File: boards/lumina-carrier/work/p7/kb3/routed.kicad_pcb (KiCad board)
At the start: 4 copper layers, 100 x 80 mm, 116 parts, among them J1 LPJG0926HENL PoE+ RJ45 magjack, J2 1x6 2.54mm header (recovery), J3 DS1021-2x7SF11-B 2x7 male hea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, J4 DS1021-2x12SF11-B 2x12 male h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, SW1 SMD tactile switch, U1 TPS2378DDAR, U10 W5500, U20 SCT2A25STER, U21 TPS563201DDCR, U22 TPS16630PWPR, U30 ESP32-S3-WROOM-1-N8, Y10 25MHz 18pF CL crystal

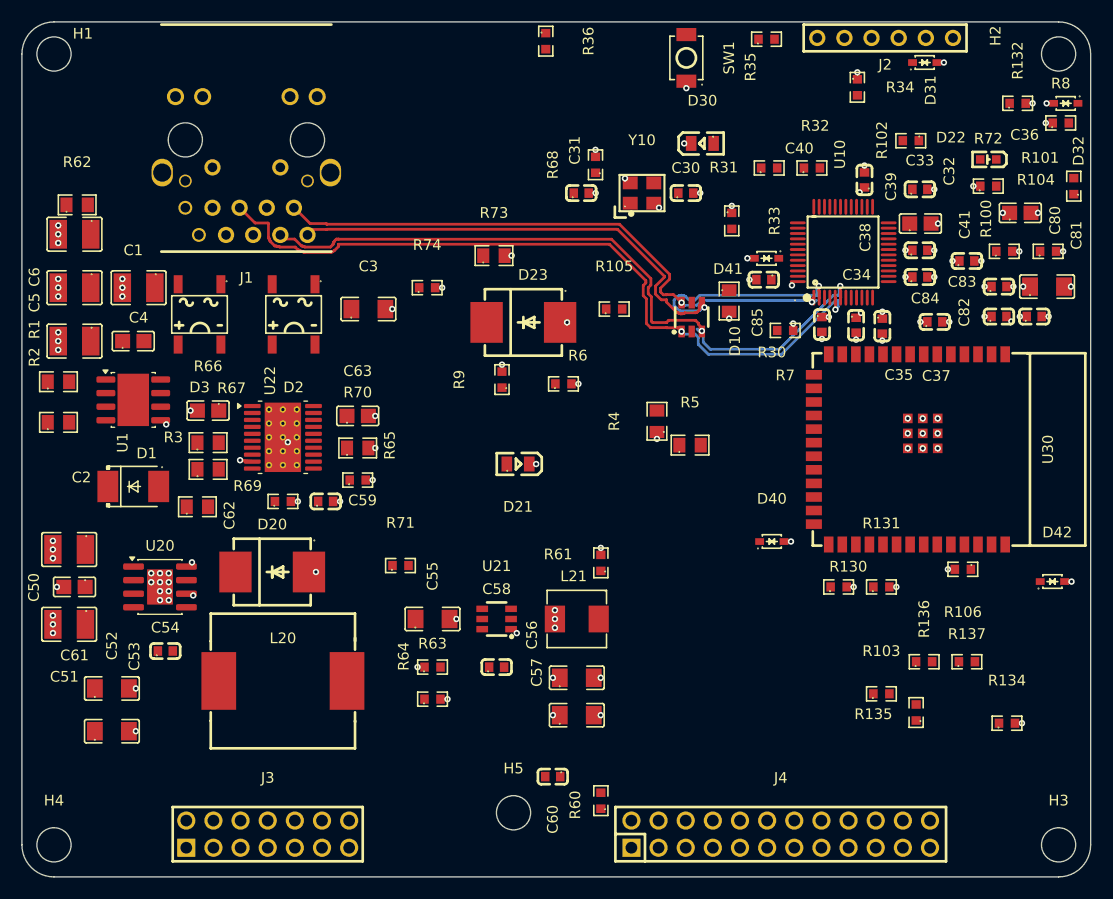
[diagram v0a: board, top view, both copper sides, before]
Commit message: ai-ee lumina-carrier: P7 partial - planes, rule areas, MDI pairs, thermal stitching (177 unrouted)
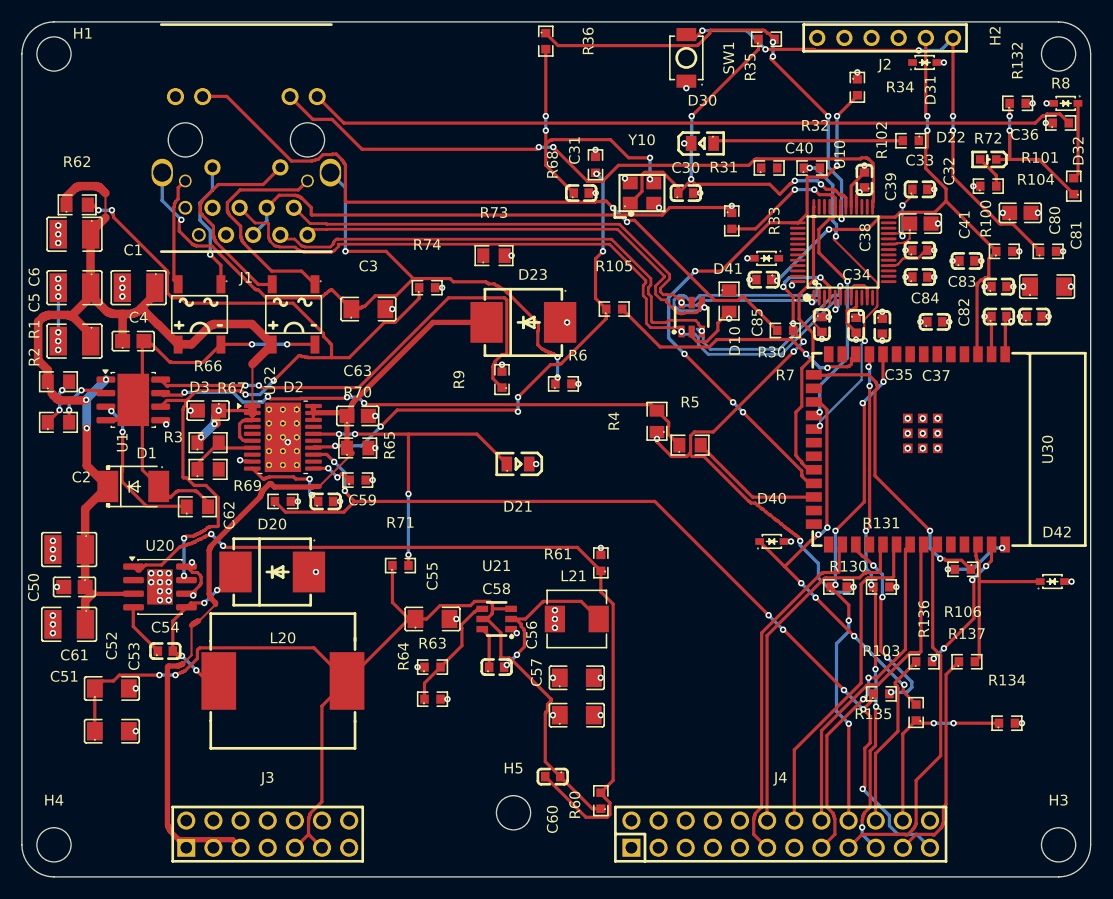
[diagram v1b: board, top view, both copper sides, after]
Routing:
- net +3V3: track 5.20 -> 119.2 mm, vias 31 -> 36
- net V48_RAW: track 0.00 -> 110.4 mm, vias 0 -> 6
- net +12V: track 0.00 -> 99.9 mm, vias 0 -> 2
- net /ENABLE: track 0.00 -> 89.5 mm, vias 0 -> 7
- net /CDB: track 0.00 -> 82.8 mm, vias 0 -> 6
- net +48V_SW: track 0.00 -> 81.2 mm
- net /pwr/FB48: track 0.00 -> 78.5 mm, vias 0 -> 2
- net /poe/LED_G_A: track 0.00 -> 72.1 mm
- net /poe/SHIELD: track 0.00 -> 68.9 mm, vias 0 -> 4
- net /poe/LED_Y_A: track 0.00 -> 65.9 mm, vias 0 -> 2
- net /ETH_LED_LINK: track 0.00 -> 63.3 mm, vias 0 -> 2
- net /ETH_RSTn: track 0.00 -> 53.5 mm, vias 0 -> 6
- net /mcu/EN: track 0.00 -> 53.1 mm, vias 0 -> 4
- net /poe/T2P_OD: track 0.00 -> 51.9 mm, vias 0 -> 4
- net /mcu/BOOT: track 0.00 -> 50.7 mm, vias 0 -> 5
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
